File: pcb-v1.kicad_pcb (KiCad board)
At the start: 2 copper layers, 7 parts, among them J1 Conn_01x03_Socket, J2 Conn_01x03_Socket, J3 Conn_01x03_Socket, J4 Conn_01x03_Socket, J5 Conn_01x03_Socket, J6 Conn_01x03_Socket

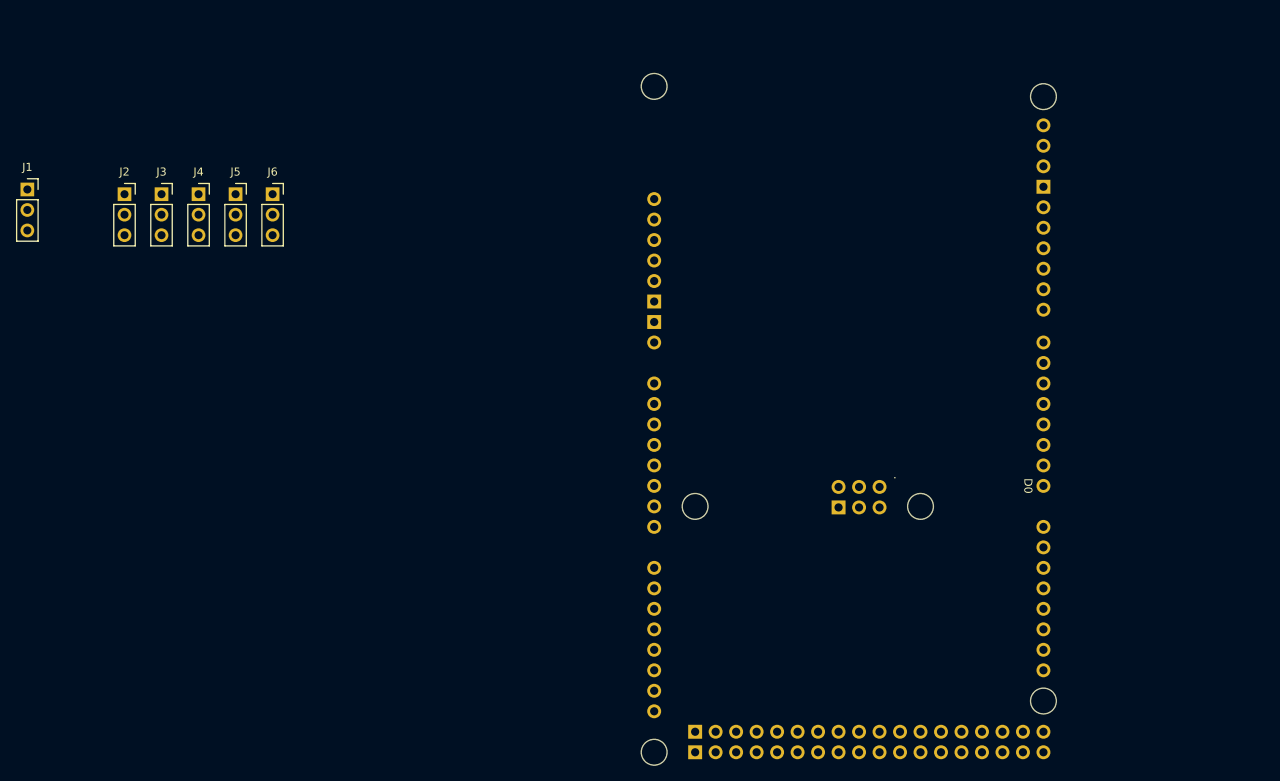
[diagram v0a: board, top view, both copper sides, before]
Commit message: add all symbol and footprint
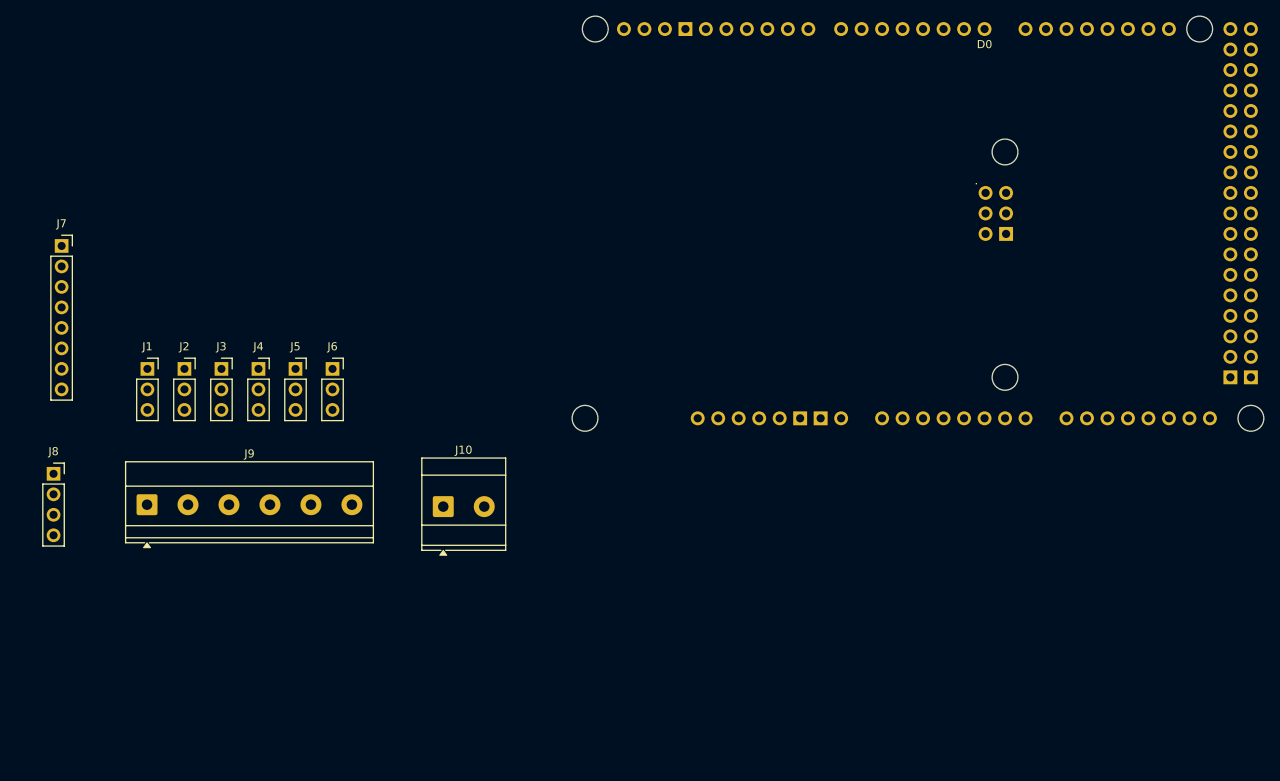
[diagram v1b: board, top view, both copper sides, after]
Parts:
- added J10: Screw_Terminal_01x02, TerminalBlock_Phoenix:TerminalBlock_Phoenix_MKDS-3-2-5.08_1x02_P5.08mm_Horizontal, F.Cu at (163.3, 106.0)
- added J7: Conn_01x08_Socket, Connector_PinSocket_2.54mm:PinSocket_1x08_P2.54mm_Vertical, F.Cu at (116.0, 73.7)
- added J8: Conn_01x04_Socket, Connector_PinSocket_2.54mm:PinSocket_1x04_P2.54mm_Vertical, F.Cu at (115.0, 101.9)
- added J9: Screw_Terminal_01x06, TerminalBlock_Phoenix:TerminalBlock_Phoenix_MKDS-1,5-6-5.08_1x06_P5.08mm_Horizontal, F.Cu at (126.6, 105.8)
- moved A1 61.0 mm to (166.9, 97.6), turned to 0 degrees
- moved J1 26.8 mm to (126.6, 88.9)
- moved J3 22.9 mm to (135.8, 88.9)
- moved J4 22.9 mm to (140.4, 88.9)
- moved J5 22.9 mm to (145.0, 88.9)
- moved J6 22.9 mm to (149.6, 88.9)
- moved J2 22.9 mm to (131.2, 88.9)
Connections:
- A1 pad 3V3: unconnected-(A1-3.3V-Pad3V3) -> /3.3VDC
- A1 pad 5V1: unconnected-(A1-5V-Pad5V1) -> /5VDC
- A1 pad 5V3: unconnected-(A1-5V-Pad5V3) -> /5VDC
- A1 pad 5V4: unconnected-(A1-5V-Pad5V4) -> /5VDC
- A1 pad A0: unconnected-(A1-PadA0) -> /Belt
- A1 pad A1: unconnected-(A1-PadA1) -> /L-Lamp
- A1 pad A2: unconnected-(A1-PadA2) -> /R-Lamp
- A1 pad A3: unconnected-(A1-PadA3) -> /Park
- A1 pad A4: unconnected-(A1-PadA4) -> /Gear
- A1 pad A5: unconnected-(A1-PadA5) -> /Engine
- A1 pad D18: unconnected-(A1-D18/TX1-PadD18) -> /TX1
- A1 pad D19: unconnected-(A1-D19/RX1-PadD19) -> /RX1
- A1 pad D20: unconnected-(A1-D20/SDA-PadD20) -> /SDA
- A1 pad D21: unconnected-(A1-D21/SCL-PadD21) -> /SCL
- A1 pad D7: unconnected-(A1-PadD7) -> Net-(J9-Pin_1)
- A1 pad D8: unconnected-(A1-PadD8) -> Net-(J9-Pin_2)
- A1 pad GND1: unconnected-(A1-GND-PadGND1) -> GND
- A1 pad GND2: unconnected-(A1-GND-PadGND2) -> GND
- A1 pad GND3: unconnected-(A1-GND-PadGND3) -> GND
- A1 pad GND4: unconnected-(A1-SPI_GND-PadGND4) -> GND
- A1 pad GND5: unconnected-(A1-GND-PadGND5) -> GND
- A1 pad GND6: unconnected-(A1-GND-PadGND6) -> GND
- A1 pad VIN: unconnected-(A1-PadVIN) -> /VIN
- J1 pad 1: unconnected-(J1-Pin_1-Pad1) -> /Belt
- J1 pad 2: unconnected-(J1-Pin_2-Pad2) -> /5VDC
- J1 pad 3: unconnected-(J1-Pin_3-Pad3) -> GND
- J2 pad 1: unconnected-(J2-Pin_1-Pad1) -> /L-Lamp
- J2 pad 2: unconnected-(J2-Pin_2-Pad2) -> /5VDC
- J2 pad 3: unconnected-(J2-Pin_3-Pad3) -> GND
- J3 pad 1: unconnected-(J3-Pin_1-Pad1) -> /R-Lamp
- J3 pad 2: unconnected-(J3-Pin_2-Pad2) -> /5VDC
- J3 pad 3: unconnected-(J3-Pin_3-Pad3) -> GND
- J4 pad 1: unconnected-(J4-Pin_1-Pad1) -> /Park
- J4 pad 2: unconnected-(J4-Pin_2-Pad2) -> /5VDC
- J4 pad 3: unconnected-(J4-Pin_3-Pad3) -> GND
- J5 pad 1: unconnected-(J5-Pin_1-Pad1) -> /Gear
- J5 pad 2: unconnected-(J5-Pin_2-Pad2) -> /5VDC
- J5 pad 3: unconnected-(J5-Pin_3-Pad3) -> GND
- J6 pad 1: unconnected-(J6-Pin_1-Pad1) -> /Engine
- J6 pad 2: unconnected-(J6-Pin_2-Pad2) -> /5VDC
- J6 pad 3: unconnected-(J6-Pin_3-Pad3) -> GND

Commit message: before routing
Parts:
- added H1: MountingHole, MountingHole:MountingHole_4.5mm, F.Cu at (165.3, 21.6)
- added H10: MountingHole, MountingHole:MountingHole_4.5mm, F.Cu at (60.2, 184.0)
- added H11: MountingHole, MountingHole:MountingHole_4.5mm, F.Cu at (60.2, 17.2)
- added H12: MountingHole, MountingHole:MountingHole_4.5mm, F.Cu at (246.8, 17.0)
- added H2: MountingHole, MountingHole:MountingHole_4.5mm, F.Cu at (165.3, 52.1)
- added H3: MountingHole, MountingHole:MountingHole_4.5mm, F.Cu at (225.8, 21.6)
- added H4: MountingHole, MountingHole:MountingHole_4.5mm, F.Cu at (225.8, 52.1)
- added H5: MountingHole, MountingHole:MountingHole_4.5mm, F.Cu at (69.8, 20.5)
- added H6: MountingHole, MountingHole:MountingHole_4.5mm, F.Cu at (114.3, 20.5)
- added H7: MountingHole, MountingHole:MountingHole_4.5mm, F.Cu at (69.8, 88.5)
- added H8: MountingHole, MountingHole:MountingHole_4.5mm, F.Cu at (114.3, 88.5)
- added H9: MountingHole, MountingHole:MountingHole_4.5mm, F.Cu at (246.8, 184.2)
- added J11: Screw_Terminal_01x04, TerminalBlock_Phoenix:TerminalBlock_Phoenix_MKDS-3-4-5.08_1x04_P5.08mm_Horizontal, F.Cu at (235.8, 129.8)
- added J12: Screw_Terminal_01x04, TerminalBlock_Phoenix:TerminalBlock_Phoenix_MKDS-3-4-5.08_1x04_P5.08mm_Horizontal, F.Cu at (69.3, 133.0)
- added J13: Screw_Terminal_01x04, TerminalBlock_Phoenix:TerminalBlock_Phoenix_MKDS-3-4-5.08_1x04_P5.08mm_Horizontal, F.Cu at (69.3, 156.4)
- added J14: Screw_Terminal_01x06, TerminalBlock_Phoenix:TerminalBlock_Phoenix_MKDS-3-6-5.08_1x06_P5.08mm_Horizontal, F.Cu at (69.3, 99.3)
- added J15: Conn_01x06_Pin, Connector_Molex:Molex_KK-396_A-41792-0006_1x06_P3.96mm_Horizontal, F.Cu at (85.0, 100.4)
- J10: value Screw_Terminal_01x02 -> Screw_Terminal_01x04; footprint TerminalBlock_Phoenix:TerminalBlock_Phoenix_MKDS-3-2-5.08_1x02_P5.08mm_Horizontal -> TerminalBlock_Phoenix:TerminalBlock_Phoenix_MKDS-3-4-5.08_1x04_P5.08mm_Horizontal
- J9: value Screw_Terminal_01x06 -> Conn_01x06_Pin; footprint TerminalBlock_Phoenix:TerminalBlock_Phoenix_MKDS-1,5-6-5.08_1x06_P5.08mm_Horizontal -> Connector_Molex:Molex_KK-396_A-41792-0006_1x06_P3.96mm_Horizontal
- moved J7 85.0 mm to (109.4, 158.4)
- moved J6 79.4 mm to (157.5, 167.9)
- moved J10 72.5 mm to (235.8, 102.8), turned to 90 degrees
- moved J5 64.5 mm to (157.5, 152.2)
- moved J4 50.6 mm to (157.5, 136.5)
- moved J3 38.6 mm to (157.5, 120.8)
- moved J8 34.6 mm to (105.0, 135.0)
- moved J9 33.0 mm to (130.4, 73.0)
- moved J1 30.9 mm to (157.5, 89.4)
- moved J2 30.9 mm to (157.5, 105.1)
- moved A1 21.3 mm to (166.4, 76.3), turned to -90 degrees
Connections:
- A1 pad D10: unconnected-(A1-PadD10) -> Net-(J9-Pin_6)
- A1 pad D7: Net-(J9-Pin_1) -> Net-(J9-Pin_3)
- A1 pad D8: Net-(J9-Pin_2) -> Net-(J9-Pin_4)
- A1 pad D9: unconnected-(A1-PadD9) -> Net-(J9-Pin_5)
- J10 pad 2: GND -> /VIN
- J9 pad 1: Net-(J9-Pin_1) -> /5VDC
- J9 pad 2: Net-(J9-Pin_2) -> GND
- J9 pad 3: unconnected-(J9-Pin_3-Pad3) -> Net-(J9-Pin_3)
- J9 pad 4: GND -> Net-(J9-Pin_4)
- J9 pad 5: /5VDC -> Net-(J9-Pin_5)
- J9 pad 6: GND -> Net-(J9-Pin_6)
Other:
- board outline added: 197 x 181.5 mm
- board text added: "Accerelator"
- board text added: "GPS Module"
- board text added: "Relay Module"
- board text added: "Step Down Module"
- board text added: "voltage sensor"

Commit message: ..
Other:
- board outline removed
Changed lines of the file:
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@@
 	)
 	(gr_rect
-		(start 55 12)
-		(end 252 193.5)
-		(stroke
-			(width 0.05)
-			(type default)
-		)
-		(fill no)
-		(layer "Edge.Cuts")
-	)
-	(gr_rect
-		(start 67 91.27)
-		(end 117 17.77)
+		(start 67 17.77)
+		(end 117 91.27)
 		(radius 2)
 		(stroke

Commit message: ver 1.2
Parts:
- moved J7 30.8 mm to (110.0, 127.6)
- moved J8 28.9 mm to (110.5, 163.4)
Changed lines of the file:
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@@
 	(footprint "Connector_PinSocket_2.54mm:PinSocket_1x08_P2.54mm_Vertical"
 		(layer "F.Cu")
-		(at 109.4 158.394)
+		(at 110 127.59)
 		(descr "Through hole straight socket strip, 1x08, 2.54mm pitch, single row (from Kicad 4.0.7), script generated")
 		(tags "Through hole socket strip THT 1x08 2.54mm single row")
@@
 	(footprint "Connector_PinSocket_2.54mm:PinSocket_1x04_P2.54mm_Vertical"
 		(layer "F.Cu")
-		(at 105.04 135.03)
+		(at 110.5 163.38)
 		(descr "Through hole straight socket strip, 1x04, 2.54mm pitch, single row (from Kicad 4.0.7), script generated")
 		(tags "Through hole socket strip THT 1x04 2.54mm single row")
@@
 	)
 	(gr_rect
-		(start 81.64 153.944)
-		(end 111.64 178.944)
+		(start 77.13 154.03)
+		(end 112.11 181.26)
 		(stroke
 			(width 0.1)
@@
 	)
 	(gr_rect
-		(start 81.75 129.52)
-		(end 106.75 149.52)
+		(start 98 146.58)
+		(end 112.18 126.42)
 		(stroke
 			(width 0.1)
@@
 	)
 	(gr_rect
-		(start 129.25 84.37)
+		(start 126 85.5)
 		(end 154.25 99.37)
 		(stroke
@@
 	)
 	(gr_rect
-		(start 129.25 100.15)
-		(end 154.25 115.15)
-		(stroke
-			(width 0.1)
-			(type default)
-		)
-		(fill no)
-		(layer "User.1")
-	)
-	(gr_rect
-		(start 129.25 115.93)
-		(end 154.25 130.93)
-		(stroke
-			(width 0.1)
-			(type default)
-		)
-		(fill no)
-		(layer "User.1")
-	)
-	(gr_rect
-		(start 129.25 131.71)
-		(end 154.25 146.71)
-		(stroke
-			(width 0.1)
-			(type default)
-		)
-		(fill no)
-		(layer "User.1")
-	)
-	(gr_rect
-		(start 129.25 147.49)
-		(end 154.25 162.49)
-		(stroke
-			(width 0.1)
-			(type default)
-		)
-		(fill no)
-		(layer "User.1")
-	)
-	(gr_rect
-		(start 129.25 163.27)
-		(end 154.25 178.27)
-		(stroke
-			(width 0.1)
-			(type default)
-		)
-		(fill no)
-		(layer "User.1")
-	)
-	(gr_rect
 		(start 162.52 18.88944)
 		(end 228.52 54.88944)
@@
 		(layer "User.1")
 	)
-	(gr_text "voltage sensor"
-		(at 131.15 91.87 0)
-		(layer "User.1")
-		(effects
-			(font
-				(size 2 2)
-				(thickness 0.3)
-			)
-			(justify left bottom)
-		)
-	)
-	(gr_text "voltage sensor"
-		(at 131.15 107.65 0)
-		(layer "User.1")
-		(effects
-			(font
-				(size 2 2)
-				(thickness 0.3)
-			)
-			(justify left bottom)
-		)
-	)
-	(gr_text "voltage sensor"
-		(at 131.15 123.43 0)
-		(layer "User.1")
-		(effects
-			(font
-				(size 2 2)
-				(thickness 0.3)
-			)
-			(justify left bottom)
-		)
-	)
-	(gr_text "voltage sensor"
-		(at 131.15 139.21 0)
-		(layer "User.1")
-		(effects
-			(font
-				(size 2 2)
-				(thickness 0.3)
-			)
-			(justify left bottom)
-		)
-	)
-	(gr_text "voltage sensor"
-		(at 131.15 154.99 0)
+	(gr_text "Accerelator"
+		(at 105.3 144.61 90)
 		(layer "User.1")
 		(effects
 			(font
 				(size 2 2)
-				(thickness 0.3)
+				(thickness 0.25)
 			)
 			(justify left bottom)
@@
 	)
 	(gr_text "voltage sensor"
-		(at 131.15 170.77 0)
+		(at 129.8 93.2 0)
 		(layer "User.1")
 		(effects
@@
 		)
 	)
-	(gr_text "Accerelator"
-		(at 81.75 140.77 0)
-		(layer "User.1")
-		(effects
-			(font
-				(size 3 3)
-				(thickness 0.4)
-			)
-			(justify left bottom)
-		)
-	)
 	(gr_text "GPS Module"
-		(at 83.74 167.144 0)
+		(at 80.81 168.86 0)
 		(layer "User.1")
 		(effects
@@
 	)
 	(group ""
-		(members "9a661046-9a54-4603-b252-cdba81882945" "f3633f23-b6b7-4d05-a67e-35733883ef96")
-	)
-	(group ""
 		(members "befe445e-9eb7-43ca-a6f4-29b50f626e70" "c5210d35-c1ea-41ba-aaa8-56bc6aa75656")
 	)
 	(group ""
-		(members "3de69fe3-9d1d-4850-bd3a-1bda512c6187" "b88de98c-d802-47c7-a422-cc1ad6d197e2")
-	)
-	(group ""
-		(members "2ad4b42f-cf03-41a7-aaed-46bdff86e923" "a8e2beb0-efb2-454a-9889-25d049f9d8da")
-	)
-	(group ""
-		(members "8c2487a9-4262-4f9f-b175-8747c672ee80" "cf8496c2-8fea-40ae-afac-a23101119a33")
-	)
-	(group ""
-		(members "6829f7a8-f2cc-491e-9833-4640d39be435" "cbb6dacd-250a-40c7-86b9-f24e084c8672")
-	)
-	(group ""
 		(members "445cf5ca-5192-451f-a95d-3d8ad34b3704" "f008e5fb-e611-403b-ae53-922778b261ba")
 	)
-	(group ""
-		(members "916e6ba7-9023-4e55-8009-01296f1b12e2" "aaaf84f7-9345-4524-b3ca-0763d5d35909")
-	)
 	(embedded_fonts no)

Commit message: add part finish
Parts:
- added H13: MountingHole, MountingHole:MountingHole_4.5mm, F.Cu at (67.5, 33.2)
- added H14: MountingHole, MountingHole:MountingHole_4.5mm, F.Cu at (111.0, 107.5)
- added H15: MountingHole, MountingHole:MountingHole_4.5mm, F.Cu at (234.8, 33.2)
- added H16: MountingHole, MountingHole:MountingHole_4.5mm, F.Cu at (67.5, 173.0)
- H1, H2, H3, H4, H5, H6, H7, H8: footprint MountingHole:MountingHole_4.5mm -> MountingHole:MountingHole_3.2mm_M3
- moved H11 80.2 mm to (140.2, 22.2)
- moved H10 65.5 mm to (124.8, 172.8)
- moved H12 47.9 mm to (235.2, 63.5)
- moved H9 16.6 mm to (234.8, 172.8)
- moved J13 7.44 mm to (69.3, 149.0)
- moved J12 5.45 mm to (69.3, 127.5)
- moved J8 5.40 mm to (114.2, 159.5)
- moved J10 3.75 mm to (232.0, 102.8)
- moved J11 3.75 mm to (232.0, 129.8)
- moved J14 3.32 mm to (69.3, 96.0)
- moved H5 0.95 mm to (68.8, 20.5)
- moved H6 0.95 mm to (113.3, 20.5)
- moved H7 0.95 mm to (68.8, 88.5)
- moved H8 0.95 mm to (113.3, 88.5)
- moved J7 0.50 mm to (110.0, 127.1)
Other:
- board outline added: 177 x 161.5 mm

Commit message: wiring complete
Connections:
- A1 pad 5V2: unconnected-(A1-SPI_5V-Pad5V2) -> /5VDC
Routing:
- net /5VDC: track 0.00 -> 281.5 mm
- net /SDA: track 0.00 -> 118.9 mm, vias 0 -> 1
- net /SCL: track 0.00 -> 118.8 mm, vias 0 -> 1
- net /TX1: track 0.00 -> 112.6 mm, vias 0 -> 2
- net /RX1: track 0.00 -> 110.8 mm, vias 0 -> 2
- net Net-(J9-Pin_3): track 0.00 -> 101.3 mm, vias 0 -> 1
- net Net-(J9-Pin_4): track 0.00 -> 95.6 mm
- net Net-(J9-Pin_5): track 0.00 -> 92.8 mm
- net /VIN: track 0.00 -> 87.8 mm
- net Net-(J9-Pin_6): track 0.00 -> 83.5 mm
- net GND: track 0.00 -> 72.9 mm, vias 0 -> 1
- net /3.3VDC: track 0.00 -> 66.4 mm, vias 0 -> 1
- net /L-Lamp: track 0.00 -> 44.1 mm, vias 0 -> 1
- net /Belt: track 0.00 -> 43.9 mm, vias 0 -> 1
- net /Engine: track 0.00 -> 32.9 mm
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- added copper zone on B.Cu, net GND
- added copper zone on F.Cu, net GND
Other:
- board text added: "IOBox CDT/ABD ver1.3"
